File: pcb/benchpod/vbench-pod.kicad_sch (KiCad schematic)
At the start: 109 parts, among them J1 Conn_02x10_Odd_Even, SW1 TS-1088-AR02016, SW2 TS-1088-AR02016, U1 ICE40UP5K-SG48ITR, U10 TCAN1044VDRBRQ1, U2 W25Q64JVSSIQ, U24 SN74LVC2G66DCUR, U4 ESP32-C3-MINI-1-N4, U5 STM32H563ZIT6, U7 APS6404L-3SQR-SN_C5333729, U8 TPS2116DRLR, X1 SX3M48.000B10F20TNN, Y2 Crystal_GND24

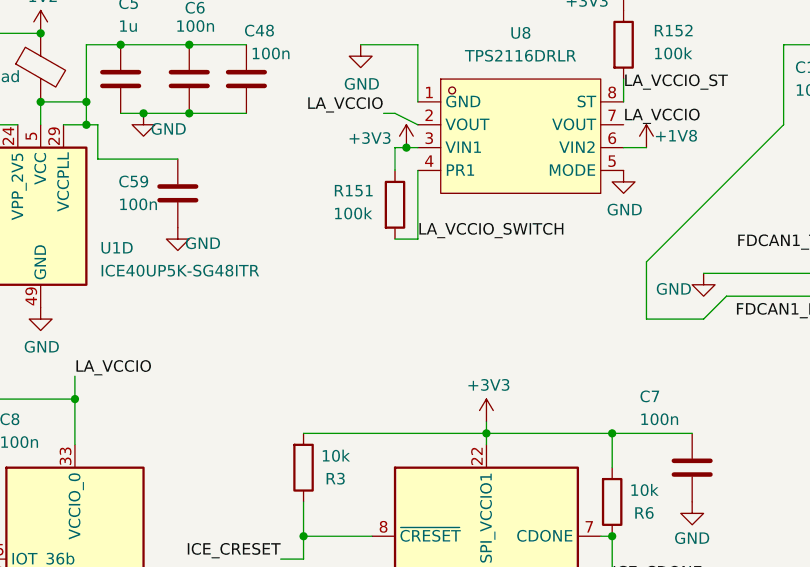
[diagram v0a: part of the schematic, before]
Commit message: 1V8/3V3 pull-ups / pull-down fixes
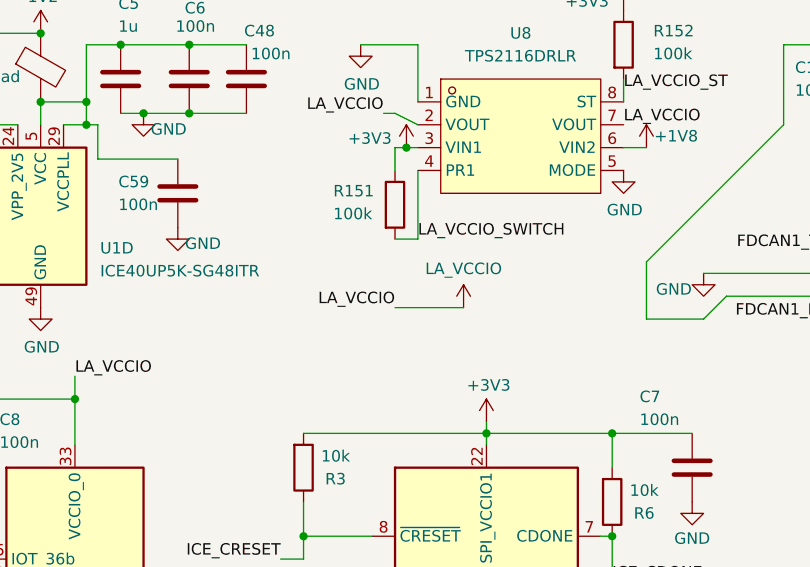
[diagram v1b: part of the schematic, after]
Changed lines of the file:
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@@
 	(wire
 		(pts
+			(xy 86.36 158.75) (xy 93.98 158.75)
+		)
+		(stroke
+			(width 0)
+			(type default)
+		)
+	)
+	(wire
+		(pts
 			(xy 76.2 184.15) (xy 83.82 184.15)
 		)
@@
 		)
 	)
+	(label "LA_VCCIO"
+		(at 86.36 158.75 180)
+		(effects
+			(font
+				(size 1.27 1.27)
+			)
+			(justify right bottom)
+		)
+	)
 	(label "CAN-"
 		(at 157.48 157.48 0)
@@
 					(unit 1)
 				)
+			)
+		)
+	)
+	(symbol
+		(lib_id "power:+3V3")
+		(at 93.98 158.75 0)
+		(unit 1)
+		(body_style 1)
+		(exclude_from_sim no)
+		(in_bom yes)
+		(on_board yes)
+		(in_pos_files yes)
+		(dnp no)
+		(property "Reference" "#PWR0349"
+			(at 93.98 162.56 0)
+			(hide yes)
+			(show_name no)
+			(do_not_autoplace no)
+			(effects
+				(font
+					(size 1.27 1.27)
+				)
+			)
+		)
+		(property "Value" "LA_VCCIO"
+			(at 93.98 154.432 0)
+			(show_name no)
+			(do_not_autoplace no)
+			(effects
+				(font
+					(size 1.27 1.27)
+				)
+			)
+		)
+		(property "Footprint" ""
+			(at 93.98 158.75 0)
+			(hide yes)
+			(show_name no)
+			(do_not_autoplace no)
+			(effects
+				(font
+					(size 1.27 1.27)
+				)
+			)
+		)
+		(property "Datasheet" ""
+			(at 93.98 158.75 0)
+			(hide yes)
+			(show_name no)
+			(do_not_autoplace no)
+			(effects
+				(font
+					(size 1.27 1.27)
+				)
+			)
+		)
+		(property "Description" "Power symbol creates a global label with name \"+3V3\""
+			(at 93.98 158.75 0)
+			(hide yes)
+			(show_name no)
+			(do_not_autoplace no)
+			(effects
+				(font
+					(size 1.27 1.27)
+				)
+			)
+		)
+		(pin "1"
+		)
+		(instances
+			(project "vbench-pod"
+				(path "/745fcf4b-2e0b-4fc4-95c0-f2e3fd40beb9"
+					(reference "#PWR0349")
+					(unit 1)
+				)

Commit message: nrst control
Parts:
- removed J1: Conn_02x10_Odd_Even, lcsc:HDR-TH_20P-P2.54-V-M-R2-C10-S2.54, symbol Connector_Generic:Conn_02x10_Odd_Even
- added J1: PZ254V-12-22P, lcsc_footprints:C492428_HDR-TH_22P-P2_54-V-M-R2-C11-S2_54, symbol lcsc_plugin:PZ254V-12-22P
- added R7: 10k, Resistor_SMD:R_0402_1005Metric, symbol Device:R
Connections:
- net +1V8: now also J1.18
- net +3V3: now also J1.17
- net CAN+: now also J1.19
- net CAN-: now also J1.20
- net GND: now also J1.15, J1.16
- net LA_INPUT1: now also J1.1
- net LA_INPUT10: now also J1.10
- net LA_INPUT11: now also J1.11
- net LA_INPUT12: now also J1.12
- net LA_INPUT13: now also J1.13
- net LA_INPUT14: now also J1.14
- net LA_INPUT2: now also J1.2
- net LA_INPUT3: now also J1.3
- net LA_INPUT4: now also J1.4
- net LA_INPUT5: now also J1.5
- net LA_INPUT6: now also J1.6
- net LA_INPUT7: now also J1.7
- net LA_INPUT8: now also J1.8
- net LA_INPUT9: now also J1.9
- net LA_VCCIO: now also J1.21, R7.1
- net NRST_CONTROL: now reaches U5.14 (PF4)
- net NRST_CONTROL: now also J1.22, R7.2
- no-connect marks 58 -> 57

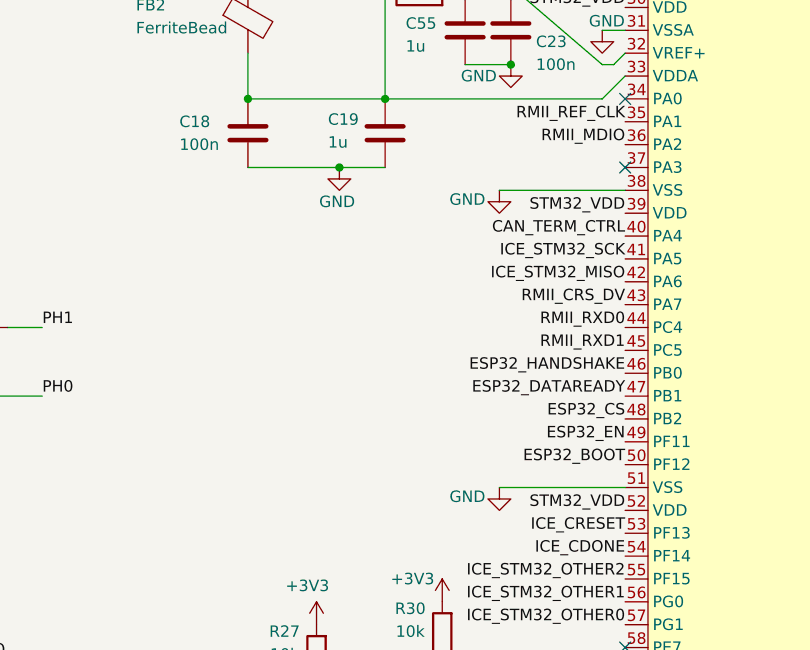
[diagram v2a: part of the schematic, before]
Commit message: replacement for crystals, revision resistors, cleanups
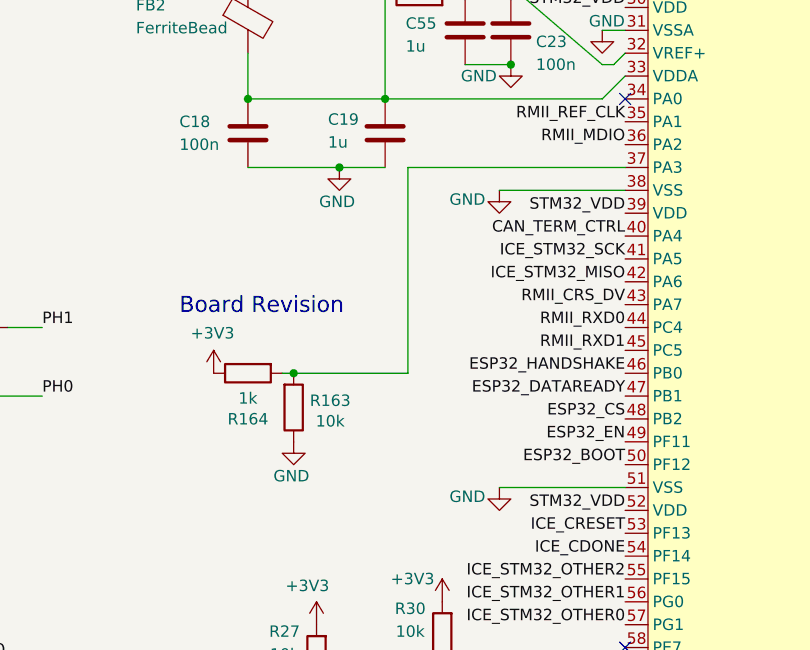
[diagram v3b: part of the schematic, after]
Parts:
- added R163: 10k, Resistor_SMD:R_0402_1005Metric, symbol Device:R
- added R164: 1k, Resistor_SMD:R_0402_1005Metric, symbol Device:R
- Y2: LCSC C20623595 -> C49867546
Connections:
- net +3V3: now also R164.1
- net GND: now also R163.1
- net at U5.37 (PA3): now also R163.2, R164.2
- no-connect marks 57 -> 56
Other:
- note added: "Board Revision"

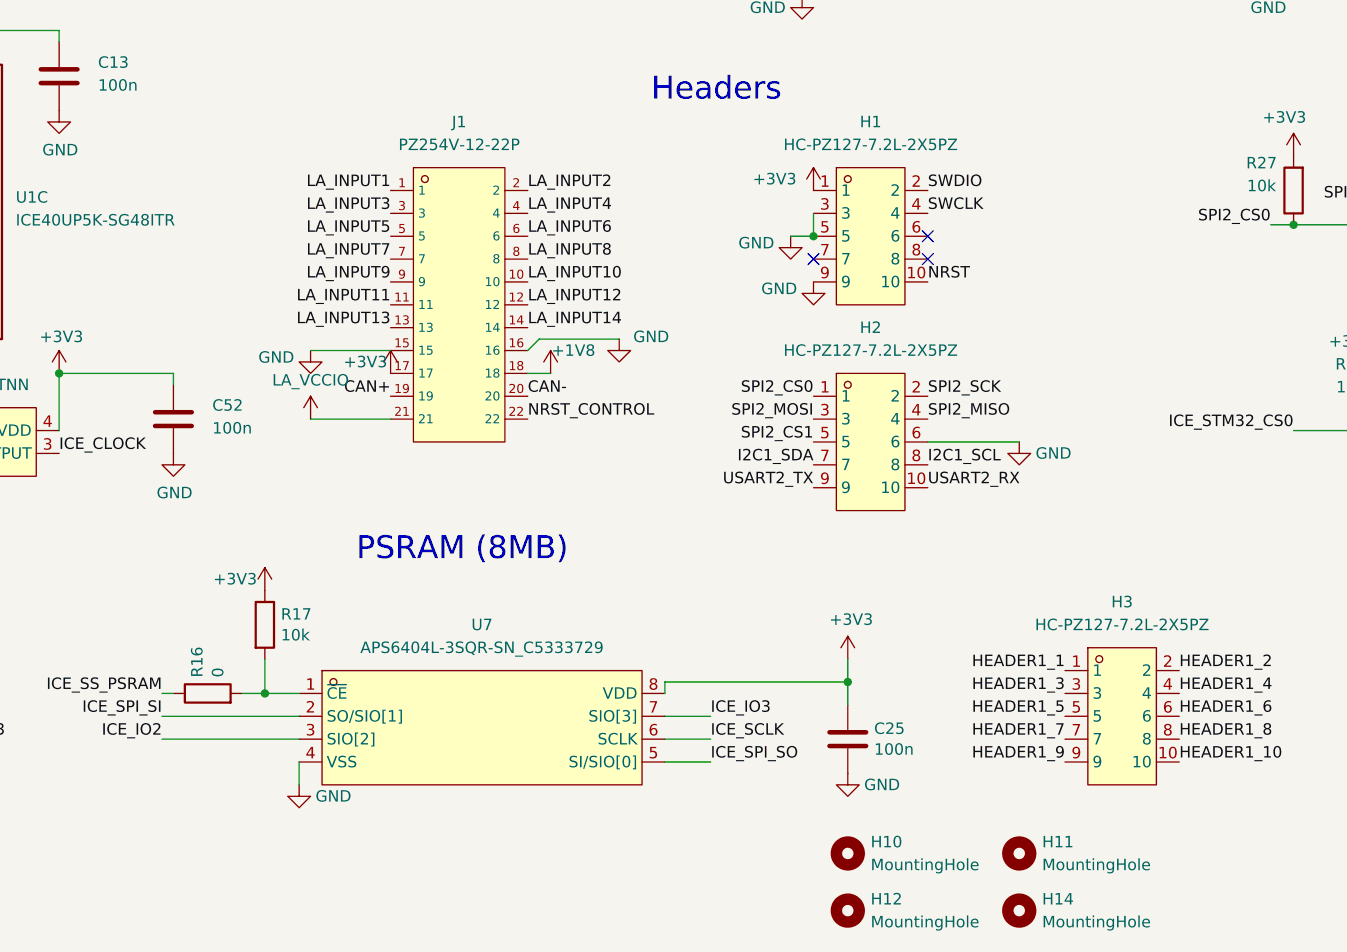
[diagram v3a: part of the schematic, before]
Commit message: route cleanups and out of stock component replacement
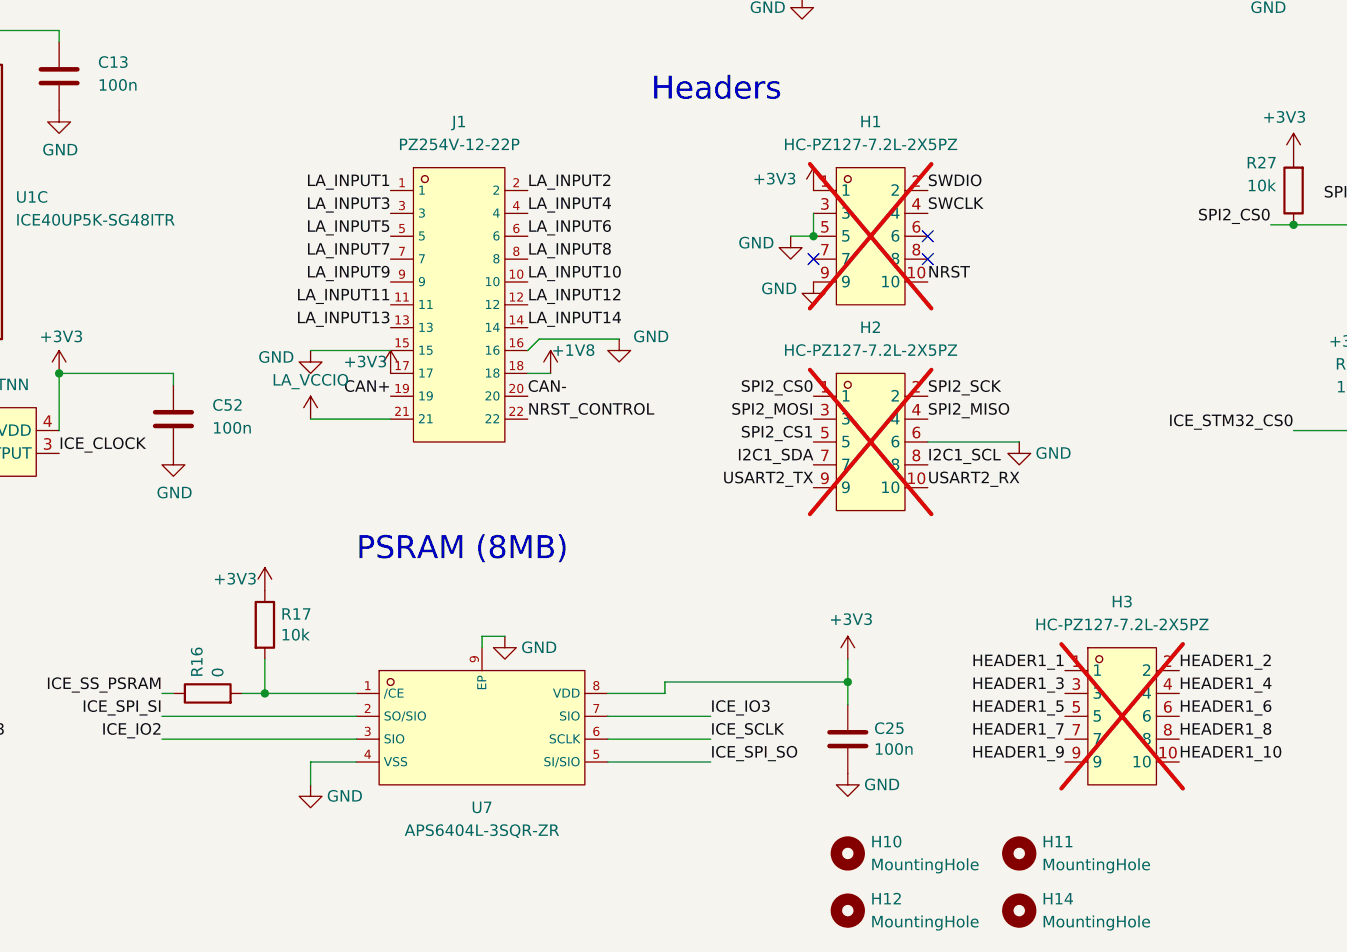
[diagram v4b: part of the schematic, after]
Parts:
- removed U7: APS6404L-3SQR-SN_C5333729, lcsc:SOIC-8_L4.9-W3.9-P1.27-LS6.0-BL, symbol lcsc_lib:APS6404L-3SQR-SN_C5333729
- added U7: APS6404L-3SQR-ZR, lcsc_footprints:C3040877_USON-8_L3_0-W2_0-P0_50-BL-EP, symbol lcsc_imported:APS6404L-3SQR-ZR
- C16: footprint Capacitor_SMD:C_0603_1608Metric -> Capacitor_SMD:C_0805_2012Metric; LCSC C59461 -> C45783
- H1, H2, H3: now not fitted
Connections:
- net +3V3: now also U7.8 (VDD)
- net GND: now also U7.4 (VSS), U7.9 (EP)
- net ICE_IO2: now also U7.3 (SIO)
- net ICE_IO3: now also U7.7 (SIO)
- net ICE_SCLK: now also U7.6 (SCLK)
- net ICE_SPI_SI: now also U7.2 (SO/SIO)
- net ICE_SPI_SO: now also U7.5 (SI/SIO)
- net at R16.2, R17.2: now also U7.1 (/CE)
